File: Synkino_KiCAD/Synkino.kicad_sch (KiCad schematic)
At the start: 162 parts, among them J1 Pwr, J10 EYE8_OUT, J11 EYE4_OUT, J12 Eye, J13 EYE5_OUT, J2 Eye, J3 3.5mm, J4 Micro_SD_Card_Det_Hirose_DM3AT, J5 EYE1_OUT, J6 EYE6_OUT, J7 EYE2_OUT, J8 EYE7_OUT, J9 EYE3_OUT, Q1 IRF7319, Q2 BC847 o. SS8050, Q3 IRLML2244 o. AO3401A, SW1 Power, SW2 Encoder, SW3 Reset, U1 ME6210A50PG, U10 ATMEGA328P-AU, U11 QRE1113GR, U12 QRE1113GR, U13 QRE1113GR, U14 QRE1113GR, U15 QRE1113GR, U16 QRE1113GR, U17 24LC256, U18 QRE1113GR, U2 ATMEGA328P-AU, U3 74HC4050, U4 SPIOLED128x64, U5 AP7312-1833W6-7, U6 74HC14, U7 VS1053B, U8 GS3005, U9 QRE1113GR, X1 FTDIconn, X2 ICSP, X3 FTDIconn, X4 ICSP, Y1 16Mhz, Y2 12.288MHz, Y3 16Mhz

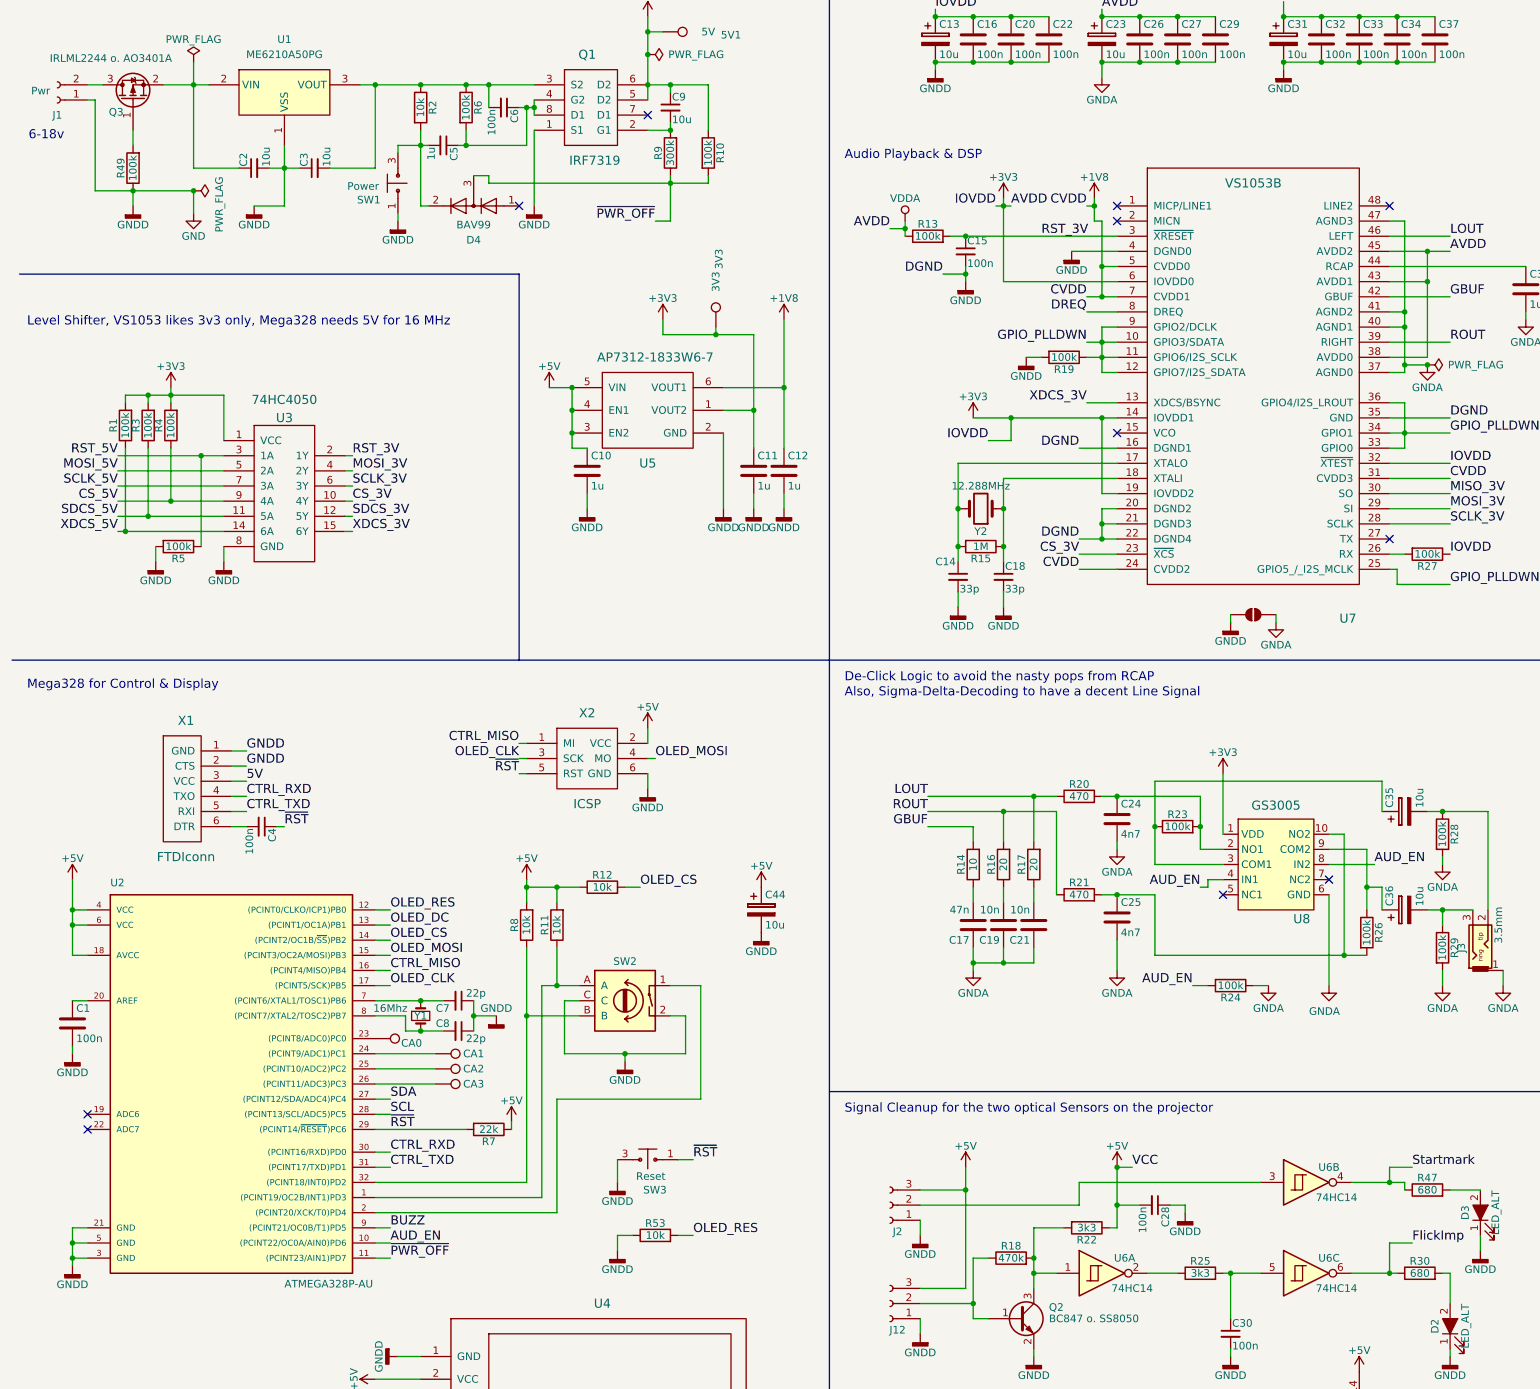
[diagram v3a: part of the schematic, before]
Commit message: Progmem Reduction Hints, D2 now white + R changed to 470
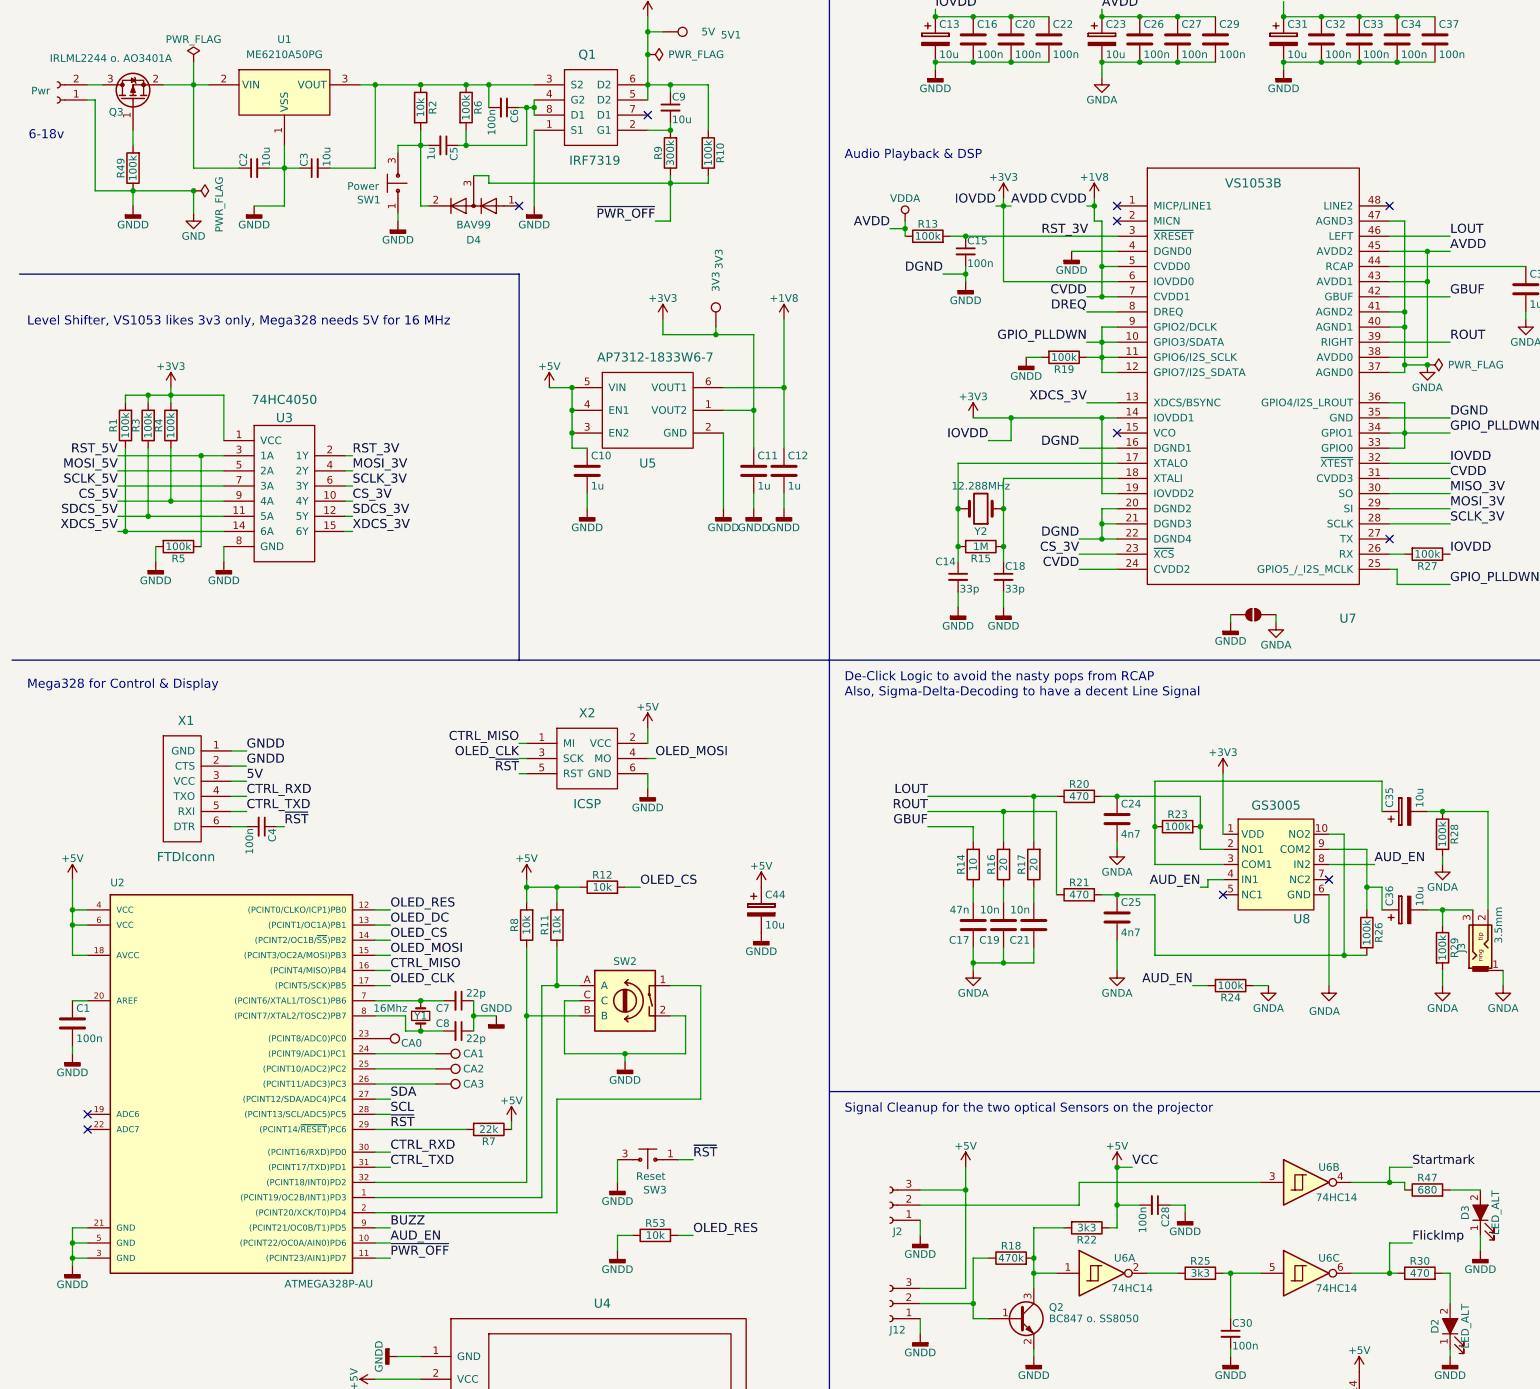
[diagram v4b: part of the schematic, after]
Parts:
- D2: LCSC C84256 -> C34499
- J1: LCSC C5188442 -> (none); Manual Assy (none) -> C5188442
- J12, J2: LCSC C5188443 -> (none); Manual Assy (none) -> C5188443
- R30: value 680 -> 470; LCSC C17798 -> C17710
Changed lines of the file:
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@@
 			)
 		)
-		(property "Value" "680"
+		(property "Value" "470"
 			(at 247.65 233.68 90)
 			(effects
@@
 			)
 		)
-		(property "LCSC" "C17798"
+		(property "LCSC" "C17710"
 			(at 247.65 233.68 0)
 			(effects
@@
 			)
 		)
-		(property "LCSC" "C84256"
+		(property "LCSC" "C34499"
 			(at 252.73 242.57 0)
 			(effects
@@
 					(size 1.27 1.27)
 				)
+				(hide yes)
 			)
 		)
@@
 			)
 		)
-		(property "LCSC" "C5188442"
+		(property "LCSC" ""
 			(at 19.05 36.83 0)
 			(effects
@@
 			)
 		)
-		(property "Manual Assy" ""
+		(property "Manual Assy" "C5188442"
 			(at 19.05 36.83 0)
 			(effects
@@
 			)
 		)
-		(property "LCSC" "C5188443"
+		(property "LCSC" ""
 			(at 158.75 222.25 0)
 			(effects
@@
 			)
 		)
-		(property "Manual Assy" ""
+		(property "Manual Assy" "C5188443"
 			(at 158.75 222.25 0)
 			(effects
@@
 			)
 		)
-		(property "LCSC" "C5188443"
+		(property "LCSC" ""
 			(at 158.75 238.76 0)
 			(effects
@@
 			)
 		)
-		(property "Manual Assy" ""
+		(property "Manual Assy" "C5188443"
 			(at 158.75 238.76 0)
 			(effects

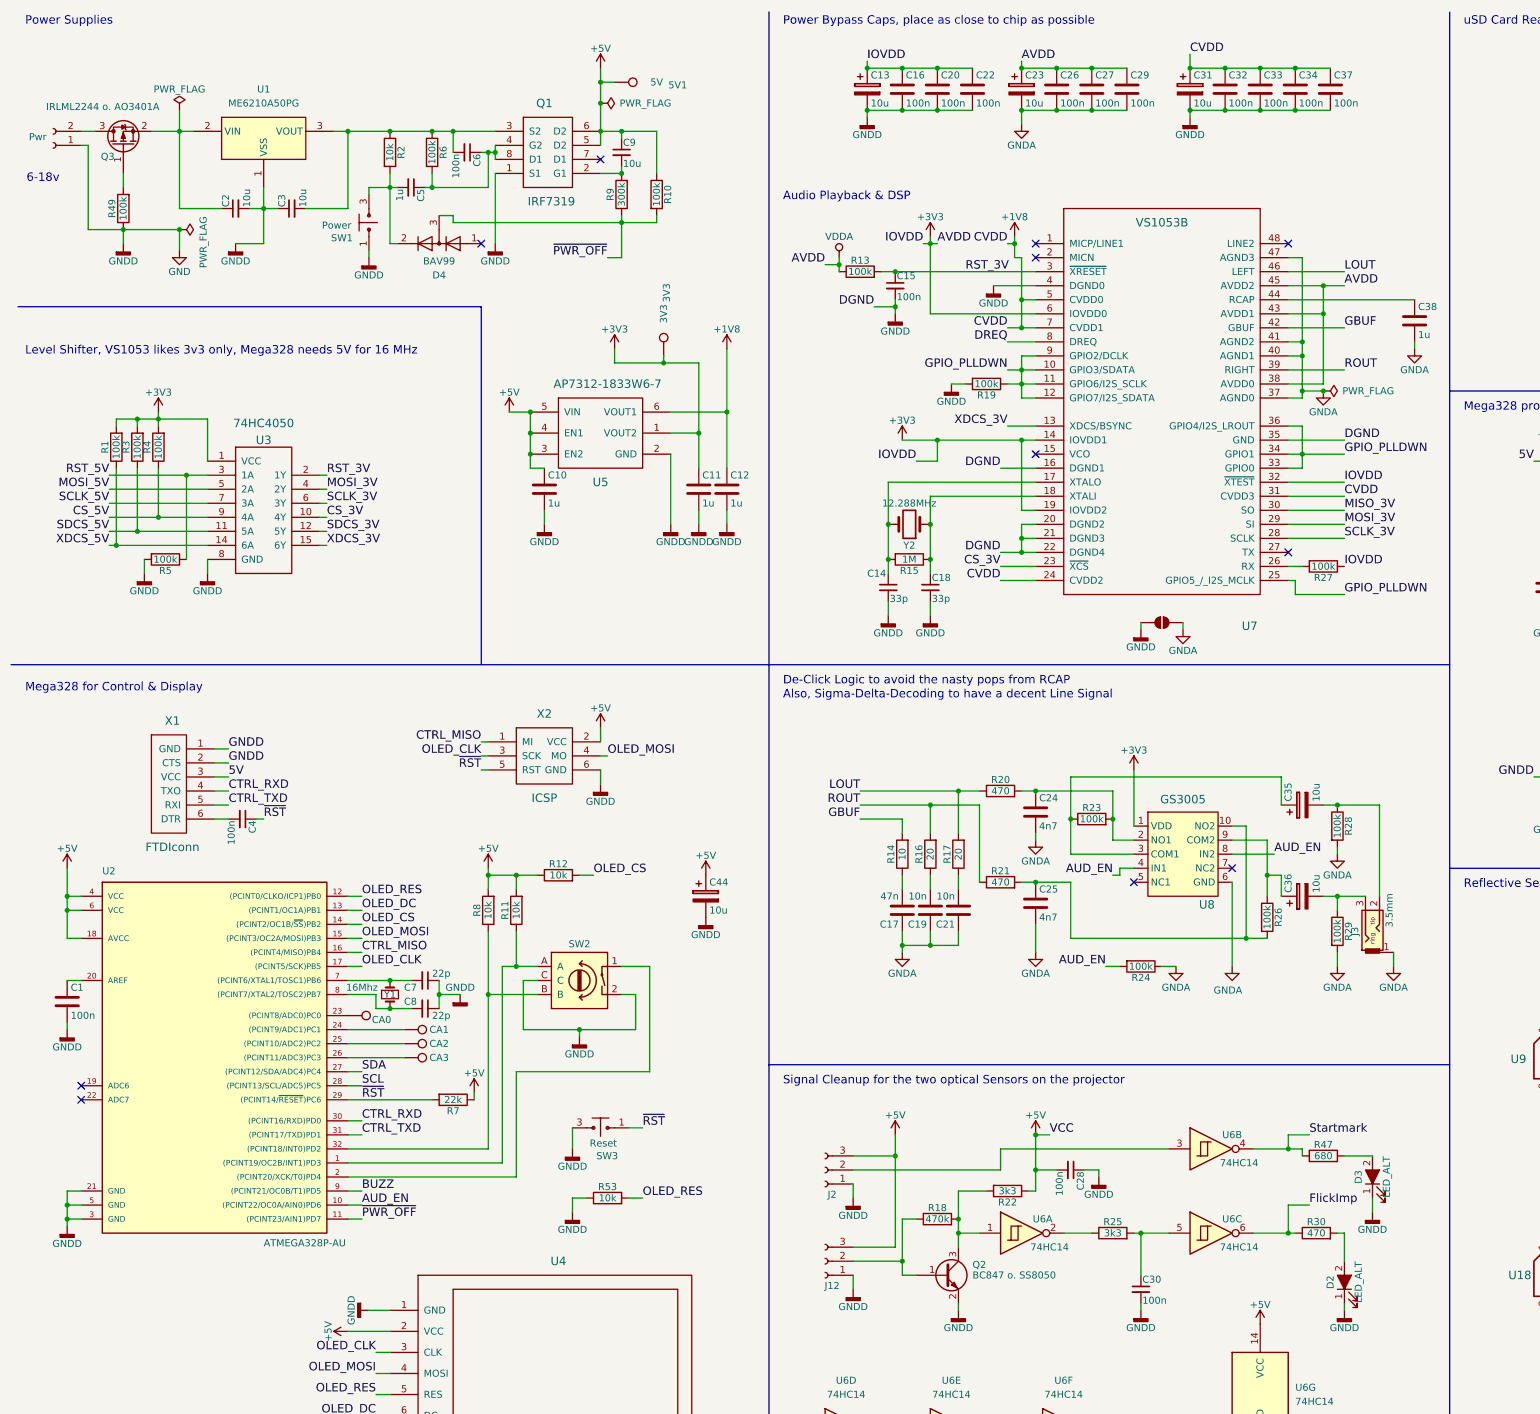
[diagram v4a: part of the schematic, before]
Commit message: Add bottom TPs for Sensor-In, Audio out and Power (test jig prep)
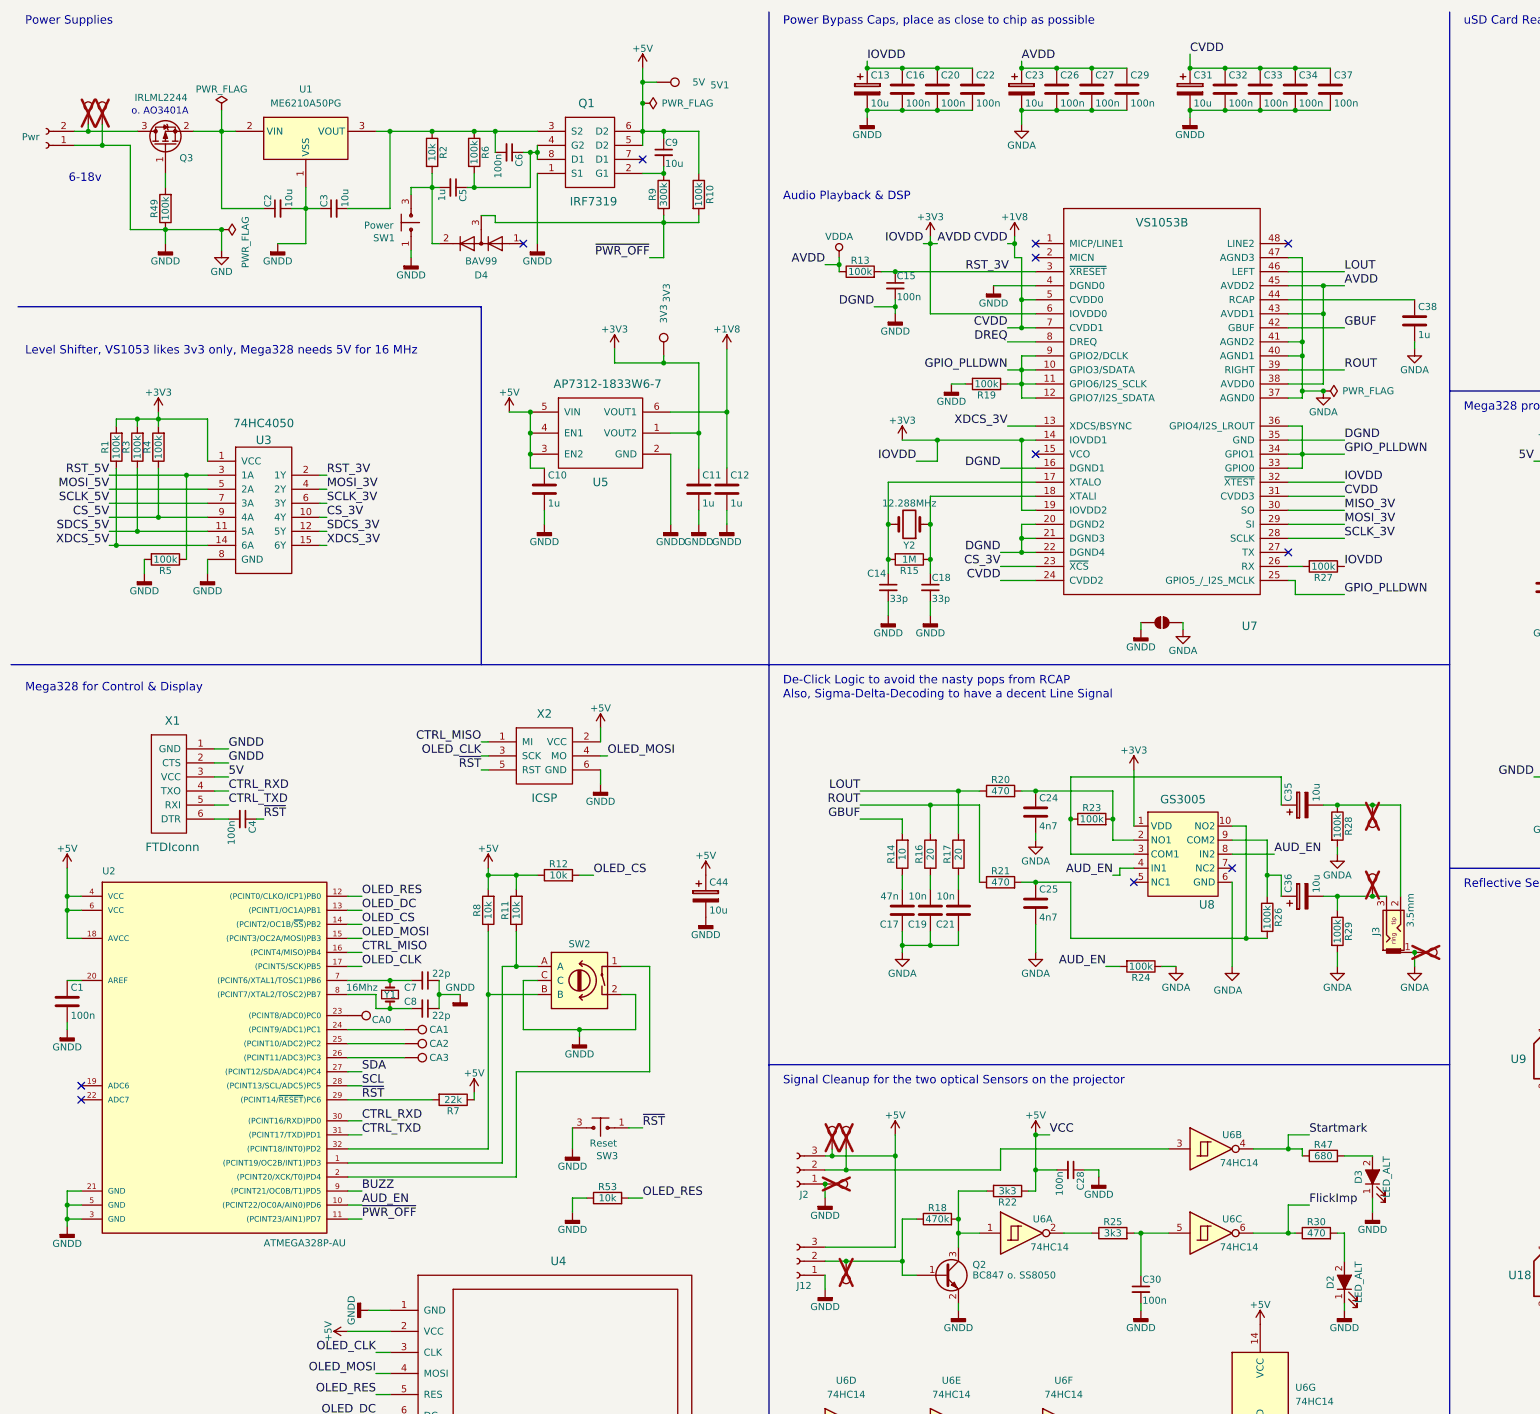
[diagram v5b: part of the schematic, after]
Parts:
- added TP1, TP2, TP3, TP4, TP5, TP6, TP7, TP8, TP9: TestPoint, Peacemans Teile:TestPoint_THTPad_1.0x1.0mm_Drill0.5mm_no_name, symbol Connector:TestPoint_no_name
- Q3: value IRLML2244 o. AO3401A -> IRLML2244
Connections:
- net +5V: now also TP1.1
- net GND: now also TP3.1, TP6.1
- net GNDA: now also TP9.1
- net at J12.2 (Pin_2), Q2.1 (B), R18.1: now also TP4.1
- net at J2.2 (Pin_2), U6.3: now also TP2.1
- net at C35.2, J3.2, R28.1: now also TP8.1
- net at C36.2, J3.3, R29.1: now also TP7.1
- net at J1.2 (Pin_2), Q3.3 (D): now also TP5.1
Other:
- note added: "o. AO3401A"
- moved on the sheet: 5V1, C2, C3, C5, C6, C9, D4, J12, J2, J3, Q1, Q3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
